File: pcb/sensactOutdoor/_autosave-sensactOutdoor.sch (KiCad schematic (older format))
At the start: 105 parts, among them J1 48V, J10 CAN, J11 EXT2, J12 CAN, J2 Conn_01x03, J3 Conn_01x03, J4 PROG, J5 LED CC, J6 PWM_OUT, J7 EXT1, J8 PWM_OUT, J9 230V, K1 ALDP105W, K2 ALDP105W, K3 ALDP105W, K4 ALDP105W, K5 ALDP105W, K6 ALDP105W, Q1 N, Q10 BC847, Q11 BC847, Q2 N, Q3 N, Q4 N, Q5 N, Q6 BC847, Q7 BC847, Q8 BC847, Q9 BC847, U1 ESP32-WROOM-32U, U2 A6211, U3 LMR16006X, U4 SN65HVD230, U5 AMS1117-3.3, U6 RF, U7 RX470B

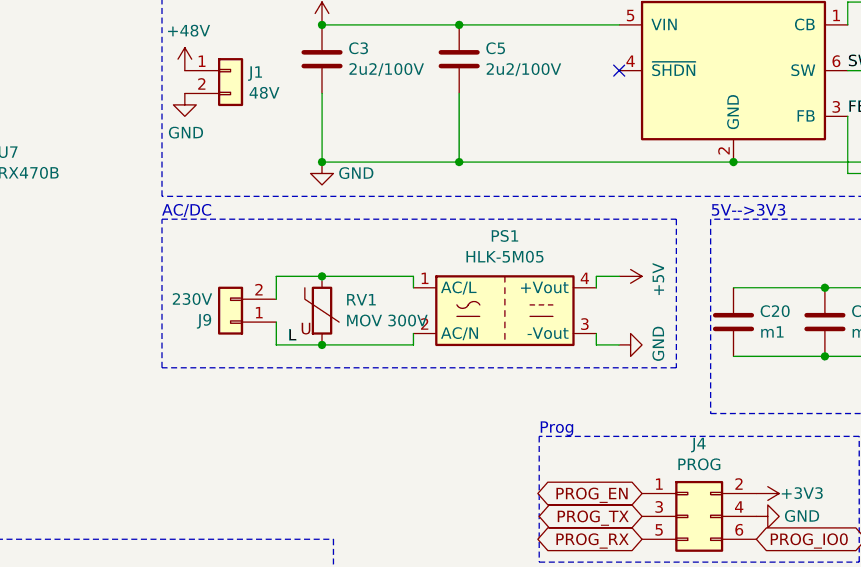
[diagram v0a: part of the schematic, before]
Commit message: added fuse , optimized routing
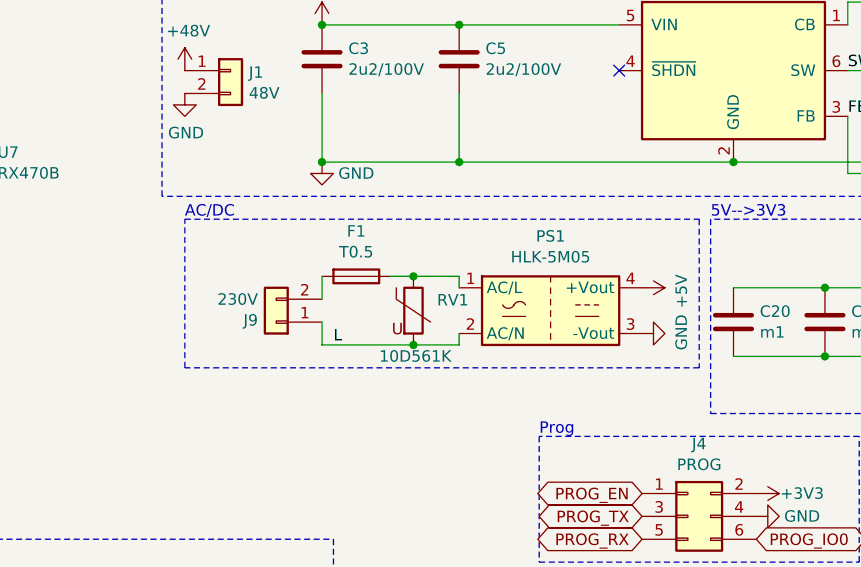
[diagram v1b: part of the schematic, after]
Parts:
- added F1: T0.5, Fuse:Fuse_Littelfuse_372_D8.50mm, symbol Device:Fuse
- RV1: value MOV 300V -> 10D561K; footprint Varistor:RV_Disc_D21.5mm_W5.8mm_P10mm -> Varistor:RV_Disc_D12mm_W6.1mm_P7.5mm
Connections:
- net at PS1.1 (AC/L), RV1.1: now also F1.1; no longer J9.2 (Pin_2)
- new net: F1.2, J9.2 (Pin_2)
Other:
- moved on the sheet: J9, PS1, RV1
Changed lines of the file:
@@
 L Converter_ACDC:HLK-PM01 PS1
 U 1 1 605A8DCF
-P 7100 3350
-F 0 "PS1" H 7100 3675 50  0000 C CNN
-F 1 "HLK-5M05" H 7100 3584 50  0000 C CNN
-F 2 "liebler_MODULES:CONV_HLK-5M05" H 7100 3050 50  0001 C CNN
-F 3 "http://www.hlktech.net/product_detail.php?ProId=54" H 7500 3000 50  0001 C CNN
-	1    7100 3350
+P 7300 3350
+F 0 "PS1" H 7300 3675 50  0000 C CNN
+F 1 "HLK-5M05" H 7300 3584 50  0000 C CNN
+F 2 "liebler_MODULES:CONV_HLK-5M05" H 7300 3050 50  0001 C CNN
+F 3 "http://www.hlktech.net/product_detail.php?ProId=54" H 7700 3000 50  0001 C CNN
+	1    7300 3350
 	1    0    0    -1
 $EndComp
@@
 L Device:Varistor RV1
 U 1 1 605A9FDB
-P 6300 3350
-F 0 "RV1" H 6403 3396 50  0000 L CNN
-F 1 "MOV 300V" H 6403 3305 50  0000 L CNN
-F 2 "Varistor:RV_Disc_D21.5mm_W5.8mm_P10mm" V 6230 3350 50  0001 C CNN
-F 3 "~" H 6300 3350 50  0001 C CNN
-	1    6300 3350
+P 6700 3350
+F 0 "RV1" H 6803 3396 50  0000 L CNN
+F 1 "10D561K" H 6550 3150 50  0000 L CNN
+F 2 "Varistor:RV_Disc_D12mm_W6.1mm_P7.5mm" V 6630 3350 50  0001 C CNN
+F 3 "~" H 6700 3350 50  0001 C CNN
+	1    6700 3350
 	1    0    0    -1
 $EndComp
@@
 L Connector_Generic:Conn_01x02 J9
 U 1 1 605AF4E9
-P 5900 3400
-F 0 "J9" H 5980 3392 50  0000 L CNN
-F 1 "230V" H 5980 3301 50  0000 L CNN
-F 2 "Connector_Phoenix_GMSTB:PhoenixContact_GMSTBVA_2,5_2-G-7,62_1x02_P7.62mm_Vertical" H 5900 3400 50  0001 C CNN
-F 3 "~" H 5900 3400 50  0001 C CNN
-	1    5900 3400
+P 6100 3400
+F 0 "J9" H 6180 3392 50  0000 L CNN
+F 1 "230V" H 6180 3301 50  0000 L CNN
+F 2 "Connector_Phoenix_GMSTB:PhoenixContact_GMSTBVA_2,5_2-G-7,62_1x02_P7.62mm_Vertical" H 6100 3400 50  0001 C CNN
+F 3 "~" H 6100 3400 50  0001 C CNN
+	1    6100 3400
 	-1   0    0    1
 $EndComp
 Wire Wire Line
-	6300 3200 6100 3200
-Wire Wire Line
-	6100 3200 6100 3300
-Wire Wire Line
-	6100 3400 6100 3500
-Wire Wire Line
-	6100 3500 6300 3500
-Wire Wire Line
-	6300 3200 6700 3200
-Wire Wire Line
-	6700 3200 6700 3250
-Connection ~ 6300 3200
+	6300 3200 6300 3300
+Wire Wire Line
+	6300 3400 6300 3500
 Wire Wire Line
 	6300 3500 6700 3500
 Wire Wire Line
-	6700 3500 6700 3450
-Connection ~ 6300 3500
+	6700 3200 6900 3200
+Wire Wire Line
+	6900 3200 6900 3250
+Wire Wire Line
+	6700 3500 6900 3500
+Wire Wire Line
+	6900 3500 6900 3450
+Connection ~ 6700 3500
 $Comp
 L power:+5V #PWR037
 U 1 1 605C7455
-P 7600 3200
-F 0 "#PWR037" H 7600 3050 50  0001 C CNN
-F 1 "+5V" H 7615 3373 50  0000 C CNN
-F 2 "" H 7600 3200 50  0001 C CNN
-F 3 "" H 7600 3200 50  0001 C CNN
-	1    7600 3200
+P 7700 3250
+F 0 "#PWR037" H 7700 3100 50  0001 C CNN
+F 1 "+5V" H 7715 3423 50  0000 C CNN
+F 2 "" H 7700 3250 50  0001 C CNN
+F 3 "" H 7700 3250 50  0001 C CNN
+	1    7700 3250
 	0    1    1    0
 $EndComp
@@
 L power:GND #PWR038
 U 1 1 605C7B08
-P 7600 3500
-F 0 "#PWR038" H 7600 3250 50  0001 C CNN
-F 1 "GND" H 7605 3327 50  0000 C CNN
-F 2 "" H 7600 3500 50  0001 C CNN
-F 3 "" H 7600 3500 50  0001 C CNN
-	1    7600 3500
-	0    -1   -1   0
-$EndComp
-Text Label 6150 3500 0    50   ~ 0
+P 7700 3450
+F 0 "#PWR038" H 7700 3200 50  0001 C CNN
+F 1 "GND" H 7705 3277 50  0000 C CNN
+F 2 "" H 7700 3450 50  0001 C CNN
+F 3 "" H 7700 3450 50  0001 C CNN
+	1    7700 3450
+	0    -1   -1   0
+$EndComp
+Text Label 6350 3500 0    50   ~ 0
 L
 Text Label 2400 3500 0    50   ~ 0
@@
 Text Label 3500 2100 3    50   ~ 0
 LED_CC-
-Wire Wire Line
-	7600 3200 7500 3200
-Wire Wire Line
-	7500 3200 7500 3250
-Wire Wire Line
-	7500 3450 7500 3500
-Wire Wire Line
-	7500 3500 7600 3500
 $Comp
 L RF:NRF24L01_Breakout U6
@@
 I2C Extension
 Wire Notes Line
-	7850 3600 5600 3600
-Wire Notes Line
-	5600 3600 5600 2950
-Wire Notes Line
-	5600 2950 7850 2950
-Wire Notes Line
-	7850 2950 7850 3600
-Text Notes 5600 2950 0    50   ~ 0
+	7950 3600 5700 3600
+Wire Notes Line
+	5700 3600 5700 2950
+Wire Notes Line
+	5700 2950 7950 2950
+Wire Notes Line
+	7950 2950 7950 3600
+Text Notes 5700 2950 0    50   ~ 0
 AC/DC
 Wire Notes Line
@@
 	4600 2700 4600 2750
 Connection ~ 4600 2700
+$Comp
+L Device:Fuse F1
+U 1 1 60502385
+P 6450 3200
+F 0 "F1" V 6253 3200 50  0000 C CNN
+F 1 "T0.5" V 6344 3200 50  0000 C CNN
+F 2 "Fuse:Fuse_Littelfuse_372_D8.50mm" V 6380 3200 50  0001 C CNN
+F 3 "~" H 6450 3200 50  0001 C CNN
+	1    6450 3200
+	0    1    1    0
+$EndComp
+Wire Wire Line
+	6700 3200 6600 3200
+Connection ~ 6700 3200
 $EndSCHEMATC
